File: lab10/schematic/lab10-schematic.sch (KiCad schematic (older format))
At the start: 15 parts, among them J1 wavegen_inputs, J2 receiver, J3 transmitter, J4 wavegen_input, U1 74LS08, U2 OPAMP, U3 OPAMP

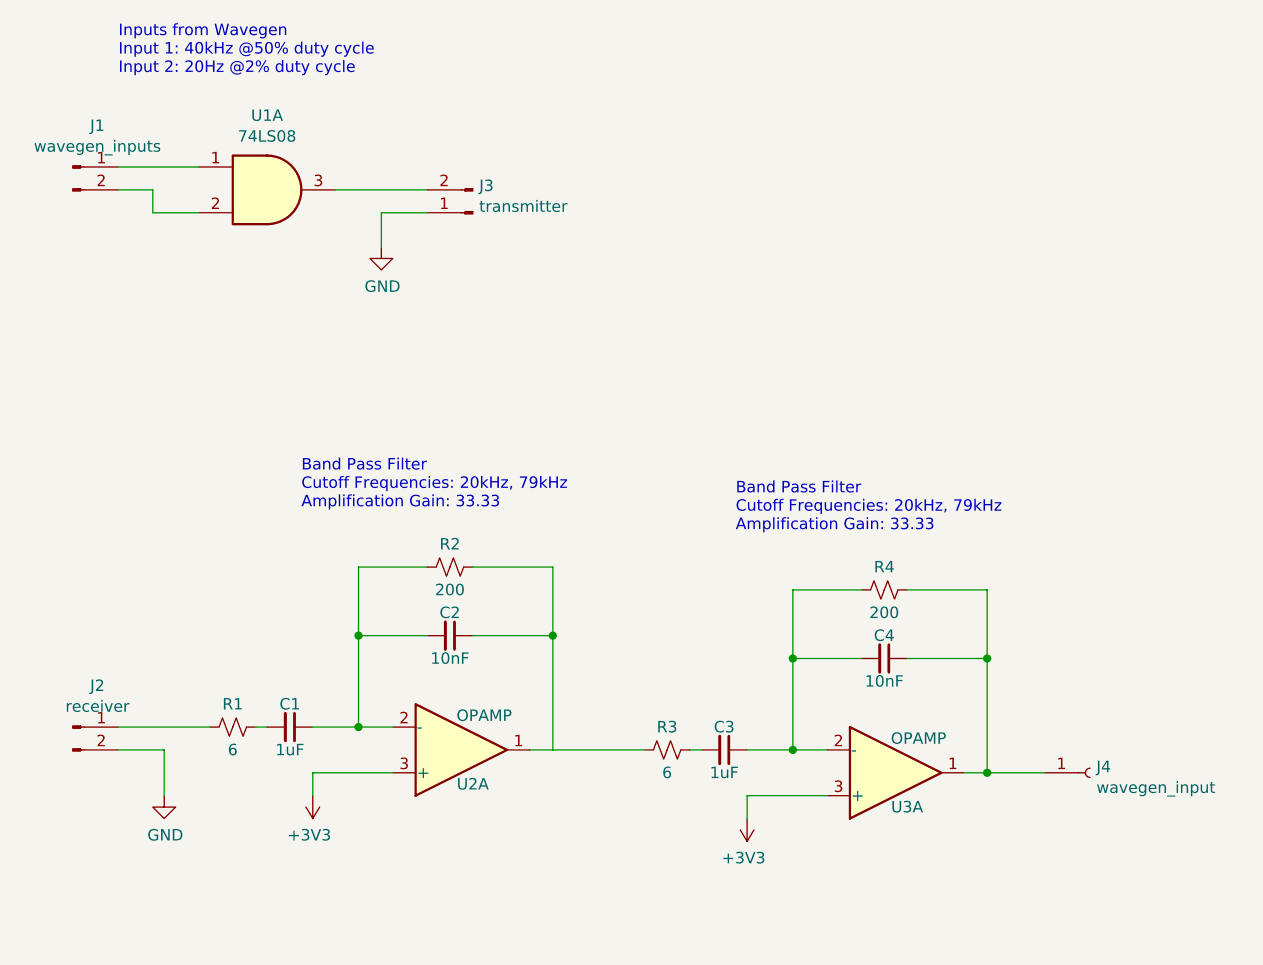
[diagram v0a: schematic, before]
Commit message: update schematic diagram ot reflect lack of 6 ohm resistors
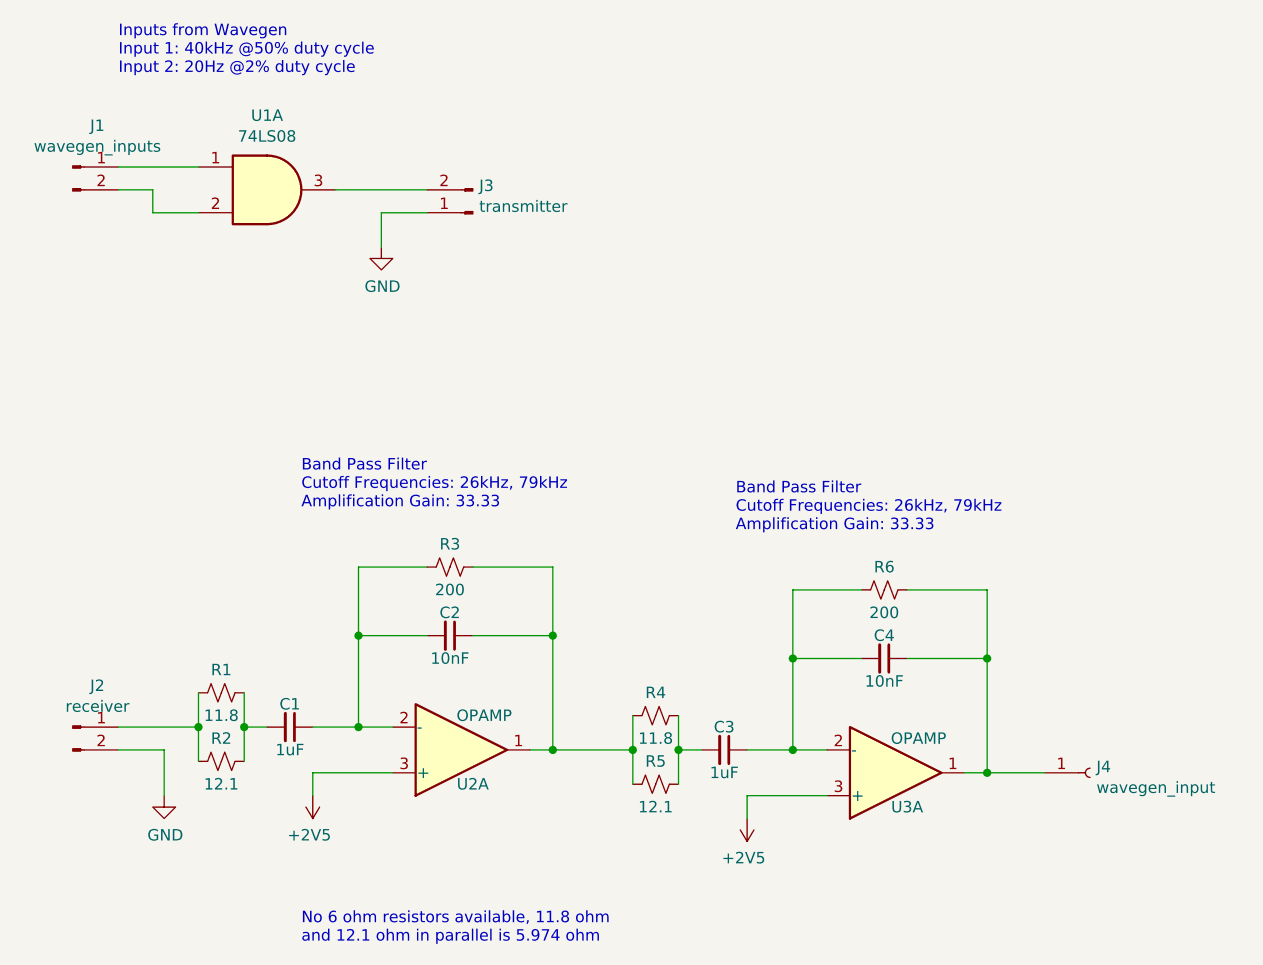
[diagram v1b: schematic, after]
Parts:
- removed R3: 6, symbol Device:R_Small_US
- added R2, R5: 12.1, symbol Device:R_Small_US
- added R4: 11.8, symbol Device:R_Small_US
- R1: value 6 -> 11.8
- renumbered R2 to R3, R4 to R6
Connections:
- net at J2.1 (Pin_1), R1.2: now also R2.2
- net at C2.1, R3.1, U2.1: now also R4.2, R5.2
- net at C1.2, R1.1: now also R2.1
- net at C3.2: now also R4.1, R5.1
- net +3V3 renamed +2V5
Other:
- note added: "Band Pass Filter\nCutoff Frequencies: 26kHz, 79kHz\nAmplification Gain: 33.33"
- note added: "No 6 ohm resistors available, 11.8 ohm\nand 12.1 ohm in parallel is 5.974 ohm"
- note removed: "Band Pass Filter\nCutoff Frequencies: 20kHz, 79kHz\nAmplification Gain: 33.33"
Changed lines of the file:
@@
 Wire Wire Line
 	3150 5150 3500 5150
-$Comp
-L Device:R_Small_US R1
-U 1 1 5DCA384B
-P 2800 4950
-F 0 "R1" V 2700 4950 50  0000 C CNN
-F 1 "6" V 2900 4950 50  0000 C CNN
-F 2 "" H 2800 4950 50  0001 C CNN
-F 3 "~" H 2800 4950 50  0001 C CNN
-	1    2800 4950
-	0    1    1    0
-$EndComp
-Wire Wire Line
-	2700 4950 2300 4950
-Wire Wire Line
-	2900 4950 2950 4950
+Wire Wire Line
+	2650 4950 2300 4950
+Wire Wire Line
+	2850 4950 2950 4950
 $Comp
 L Device:C_Small C1
@@
 $EndComp
 $Comp
-L Device:R_Small_US R2
+L Device:R_Small_US R3
 U 1 1 5DCB79EB
 P 3750 4250
-F 0 "R2" V 3650 4250 50  0000 C CNN
+F 0 "R3" V 3650 4250 50  0000 C CNN
 F 1 "200" V 3850 4250 50  0000 C CNN
 F 2 "" H 3750 4250 50  0001 C CNN
@@
 	4200 4550 4200 5050
 Text Notes 3100 4000 0    50   ~ 0
-Band Pass Filter\nCutoff Frequencies: 20kHz, 79kHz\nAmplification Gain: 33.33
+Band Pass Filter\nCutoff Frequencies: 26kHz, 79kHz\nAmplification Gain: 33.33
 $Comp
 L Amplifier_Operational:OP249 U3
@@
 Wire Wire Line
 	5050 5250 5400 5250
-$Comp
-L Device:R_Small_US R3
-U 1 1 5DCD1B30
-P 4700 5050
-F 0 "R3" V 4600 5050 50  0000 C CNN
-F 1 "6" V 4800 5050 50  0000 C CNN
-F 2 "" H 4700 5050 50  0001 C CNN
-F 3 "~" H 4700 5050 50  0001 C CNN
-	1    4700 5050
-	0    1    1    0
-$EndComp
-Wire Wire Line
-	4800 5050 4850 5050
+Wire Wire Line
+	4750 5050 4850 5050
 $Comp
 L Device:C_Small C3
@@
 $EndComp
 $Comp
-L Device:R_Small_US R4
+L Device:R_Small_US R6
 U 1 1 5DCD1B45
 P 5650 4350
-F 0 "R4" V 5550 4350 50  0000 C CNN
+F 0 "R6" V 5550 4350 50  0000 C CNN
 F 1 "200" V 5750 4350 50  0000 C CNN
 F 2 "" H 5650 4350 50  0001 C CNN
@@
 	6100 4650 6100 5150
 Text Notes 5000 4100 0    50   ~ 0
-Band Pass Filter\nCutoff Frequencies: 20kHz, 79kHz\nAmplification Gain: 33.33
-Wire Wire Line
-	4600 5050 4200 5050
+Band Pass Filter\nCutoff Frequencies: 26kHz, 79kHz\nAmplification Gain: 33.33
+Wire Wire Line
+	4550 5050 4200 5050
 $Comp
 L Connector:Conn_01x01_Female J4
@@
 Inputs from Wavegen\nInput 1: 40kHz @50% duty cycle\nInput 2: 20Hz @2% duty cycle
 $Comp
-L power:+3V3 #PWR?
-U 1 1 5DC9953C
+L power:+2V5 #PWR02
+U 1 1 5DC9CF93
 P 3150 5250
-F 0 "#PWR?" H 3150 5100 50  0001 C CNN
-F 1 "+3V3" H 3165 5423 50  0000 C CNN
+F 0 "#PWR02" H 3150 5100 50  0001 C CNN
+F 1 "+2V5" H 3165 5423 50  0000 C CNN
 F 2 "" H 3150 5250 50  0001 C CNN
 F 3 "" H 3150 5250 50  0001 C CNN
@@
 $EndComp
 $Comp
-L power:+3V3 #PWR?
-U 1 1 5DC9CA6A
+L power:+2V5 #PWR04
+U 1 1 5DC9D7E1
 P 5050 5350
-F 0 "#PWR?" H 5050 5200 50  0001 C CNN
-F 1 "+3V3" H 5065 5523 50  0000 C CNN
+F 0 "#PWR04" H 5050 5200 50  0001 C CNN
+F 1 "+2V5" H 5065 5523 50  0000 C CNN
 F 2 "" H 5050 5350 50  0001 C CNN
 F 3 "" H 5050 5350 50  0001 C CNN
@@
 	-1   0    0    1
 $EndComp
+$Comp
+L Device:R_Small_US R2
+U 1 1 5DCA4F45
+P 2750 5100
+F 0 "R2" V 2650 5100 50  0000 C CNN
+F 1 "12.1" V 2850 5100 50  0000 C CNN
+F 2 "" H 2750 5100 50  0001 C CNN
+F 3 "~" H 2750 5100 50  0001 C CNN
+	1    2750 5100
+	0    1    1    0
+$EndComp
+$Comp
+L Device:R_Small_US R1
+U 1 1 5DCA5505
+P 2750 4800
+F 0 "R1" V 2650 4800 50  0000 C CNN
+F 1 "11.8" V 2850 4800 50  0000 C CNN
+F 2 "" H 2750 4800 50  0001 C CNN
+F 3 "~" H 2750 4800 50  0001 C CNN
+	1    2750 4800
+	0    1    1    0
+$EndComp
+Wire Wire Line
+	2650 4800 2650 4950
+Connection ~ 2650 4950
+Wire Wire Line
+	2650 4950 2650 5100
+Wire Wire Line
+	2850 4800 2850 4950
+Connection ~ 2850 4950
+Wire Wire Line
+	2850 4950 2850 5100
+Connection ~ 4200 5050
+$Comp
+L Device:R_Small_US R5
+U 1 1 5DCA9F16
+P 4650 5200
+F 0 "R5" V 4550 5200 50  0000 C CNN
+F 1 "12.1" V 4750 5200 50  0000 C CNN
+F 2 "" H 4650 5200 50  0001 C CNN
+F 3 "~" H 4650 5200 50  0001 C CNN
+	1    4650 5200
+	0    1    1    0
+$EndComp
+$Comp
+L Device:R_Small_US R4
+U 1 1 5DCAA376
+P 4650 4900
+F 0 "R4" V 4550 4900 50  0000 C CNN
+F 1 "11.8" V 4750 4900 50  0000 C CNN
+F 2 "" H 4650 4900 50  0001 C CNN
+F 3 "~" H 4650 4900 50  0001 C CNN
+	1    4650 4900
+	0    1    1    0
+$EndComp
+Wire Wire Line
+	4550 4900 4550 5050
+Connection ~ 4550 5050
+Wire Wire Line
+	4550 5050 4550 5200
+Wire Wire Line
+	4750 5200 4750 5050
+Connection ~ 4750 5050
+Wire Wire Line
+	4750 5050 4750 4900
+Text Notes 3100 5900 0    50   ~ 0
+No 6 ohm resistors available, 11.8 ohm\nand 12.1 ohm in parallel is 5.974 ohm
 $EndSCHEMATC
